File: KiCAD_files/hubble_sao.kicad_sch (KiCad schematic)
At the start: 41 parts, among them J1 Conn_02x03_Counter_Clockwise, J2 Conn_02x03_Odd_Even, Q1 DMP3099L-7, SW1 SW_Push_Shielded, U1 VEML3328, U2 LSM6DSO, U3 ATmega328PB-A, U4 AD8532, U5 AD8532

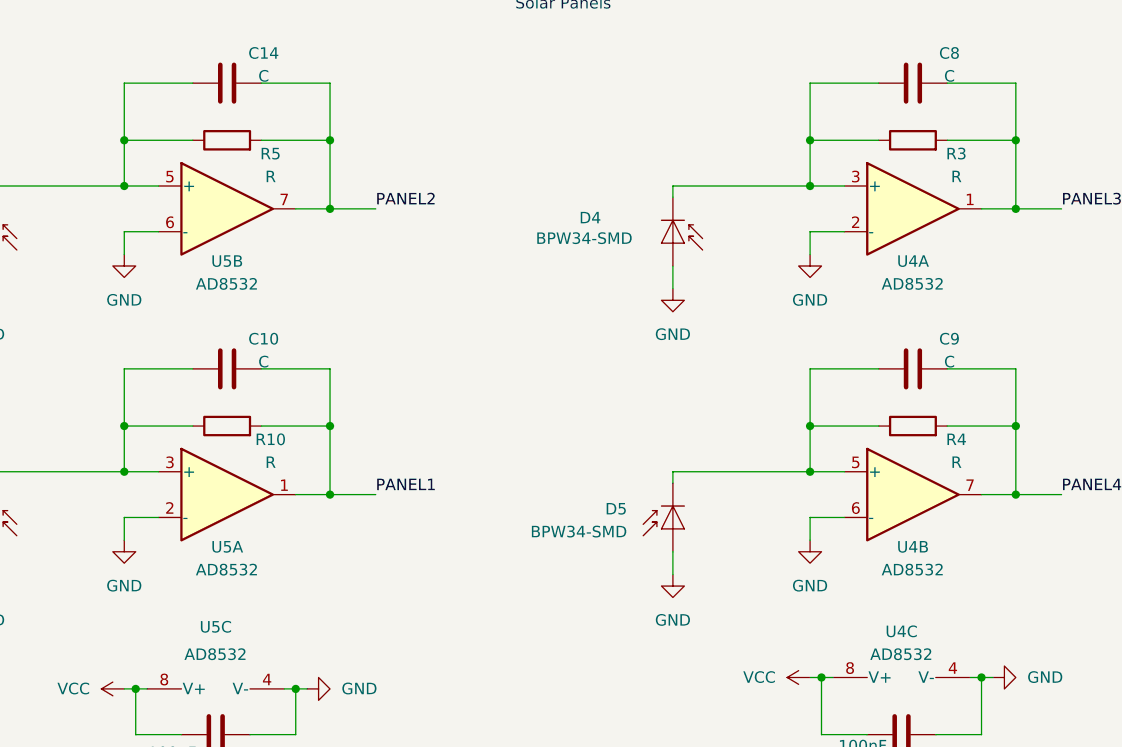
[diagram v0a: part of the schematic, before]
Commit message: Corrected the input wiring of the opamps (schematic & pcb)
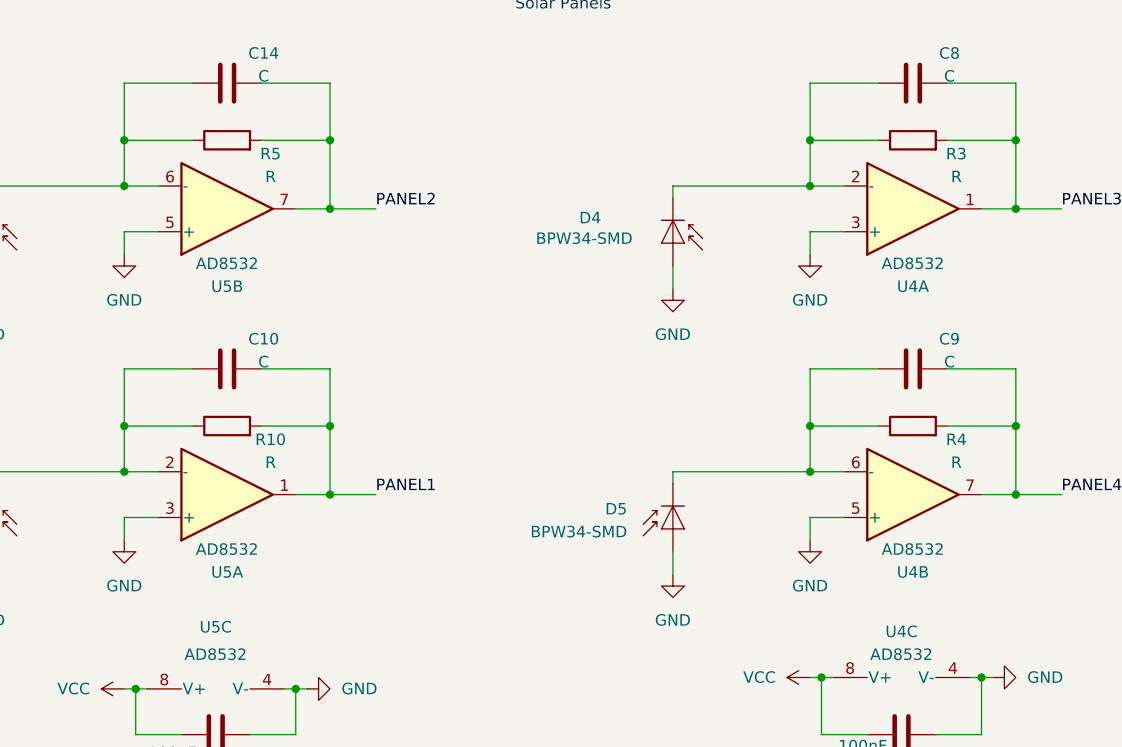
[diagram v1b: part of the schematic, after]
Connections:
- net GND: now also U4.3 (+), U4.5 (+), U5.3 (+), U5.5 (+); no longer U4.2 (-), U4.6 (-), U5.2 (-), U5.6 (-)
- net at C8.1, D4.1 (K), R3.1: now also U4.2 (-); no longer U4.3 (+)
- net at C9.1, D5.1 (K), R4.1: now also U4.6 (-); no longer U4.5 (+)
- net at C10.1, D3.1 (K), R10.1: now also U5.2 (-); no longer U5.3 (+)
- net at C14.1, D1.1 (K), R5.1: now also U5.6 (-); no longer U5.5 (+)
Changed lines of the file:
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@@
 		(lib_id "optical_sensors:AD8532")
 		(at 255.27 102.87 0)
+		(mirror x)
 		(unit 1)
 		(exclude_from_sim no)
@@
 		(dnp no)
 		(property "Reference" "U4"
-			(at 255.27 108.712 0)
+			(at 255.27 111.506 0)
 			(effects
 				(font
@@
 		)
 		(property "Value" "AD8532"
-			(at 255.27 111.252 0)
+			(at 255.27 108.966 0)
 			(effects
 				(font
@@
 		(lib_id "optical_sensors:AD8532")
 		(at 179.07 134.62 0)
+		(mirror x)
 		(unit 1)
 		(exclude_from_sim no)
@@
 		(dnp no)
 		(property "Reference" "U5"
-			(at 179.07 140.462 0)
+			(at 179.07 143.256 0)
 			(effects
 				(font
@@
 		)
 		(property "Value" "AD8532"
-			(at 179.07 143.002 0)
+			(at 179.07 140.716 0)
 			(effects
 				(font
@@
 		(lib_id "optical_sensors:AD8532")
 		(at 179.07 102.87 0)
+		(mirror x)
 		(unit 2)
 		(exclude_from_sim no)
@@
 		(dnp no)
 		(property "Reference" "U5"
-			(at 179.07 108.712 0)
+			(at 179.07 111.506 0)
 			(effects
 				(font
@@
 		)
 		(property "Value" "AD8532"
-			(at 179.07 111.252 0)
+			(at 179.07 108.966 0)
 			(effects
 				(font
@@
 		(lib_id "optical_sensors:AD8532")
 		(at 255.27 134.62 0)
+		(mirror x)
 		(unit 2)
 		(exclude_from_sim no)
@@
 		(dnp no)
 		(property "Reference" "U4"
-			(at 255.27 140.462 0)
+			(at 255.27 143.256 0)
 			(effects
 				(font
@@
 		)
 		(property "Value" "AD8532"
-			(at 255.27 143.002 0)
+			(at 255.27 140.716 0)
 			(effects
 				(font

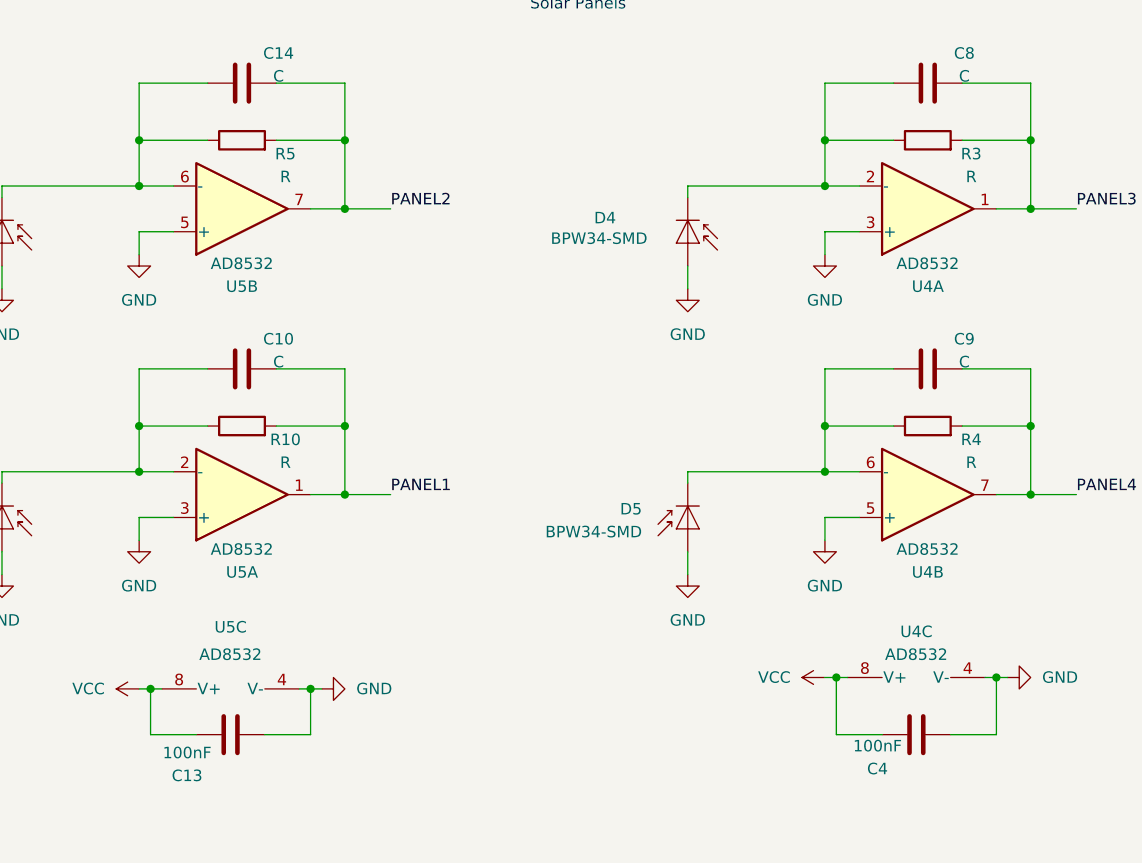
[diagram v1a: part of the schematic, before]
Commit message: Changed opamp from AD8532 to TLV9062D
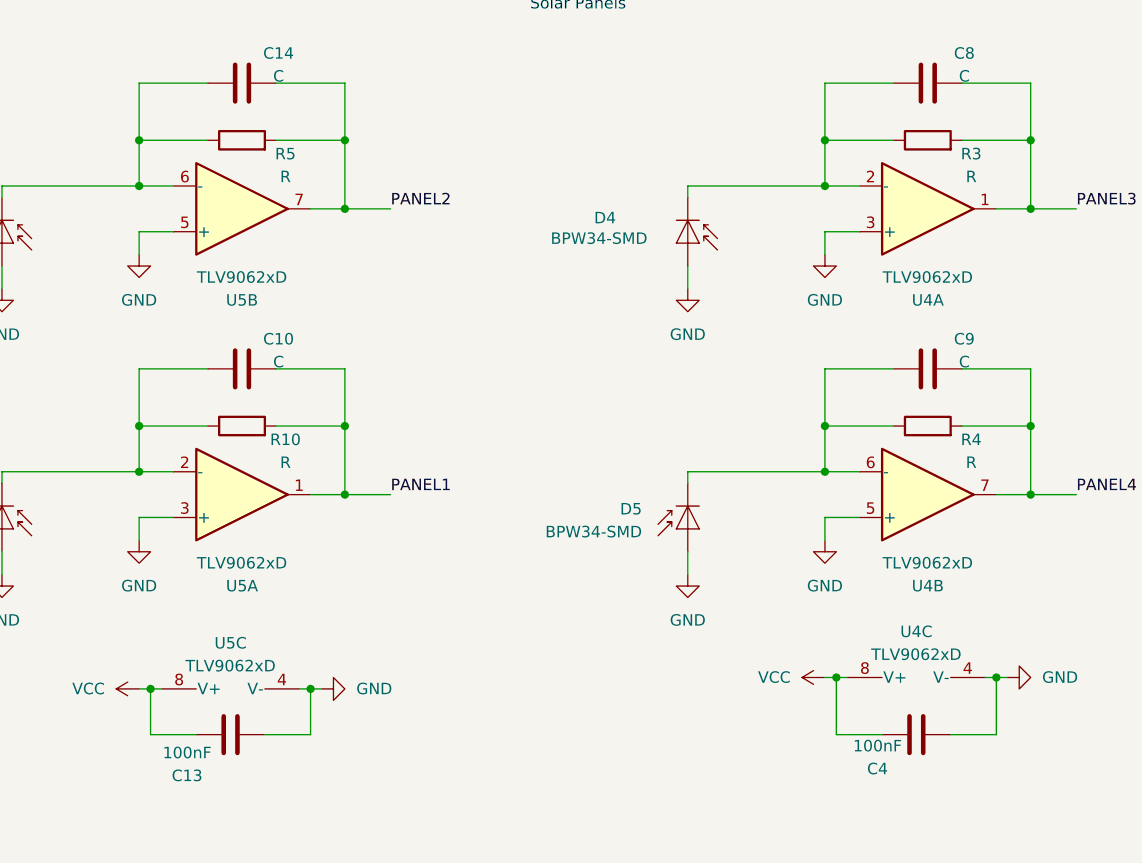
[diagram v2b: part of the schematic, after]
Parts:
- removed U4, U5: AD8532, Package_SO:SOIC-8_3.9x4.9mm_P1.27mm, symbol optical_sensors:AD8532
- added U4, U5: TLV9062xD, Package_SO:SOIC-8_3.9x4.9mm_P1.27mm, symbol Amplifier_Operational:TLV9062xD
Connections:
- net GND: now also U4.3 (+), U4.4 (V-), U4.5 (+), U5.3 (+), U5.4 (V-), U5.5 (+)
- net PANEL1: now also U5.1
- net PANEL2: now also U5.7
- net PANEL3: now also U4.1
- net PANEL4: now also U4.7
- net VCC: now also U4.8 (V+), U5.8 (V+)
- net at C8.1, D4.1 (K), R3.1: now also U4.2 (-)
- net at C9.1, D5.1 (K), R4.1: now also U4.6 (-)
- net at C10.1, D3.1 (K), R10.1: now also U5.2 (-)
- net at C14.1, D1.1 (K), R5.1: now also U5.6 (-)

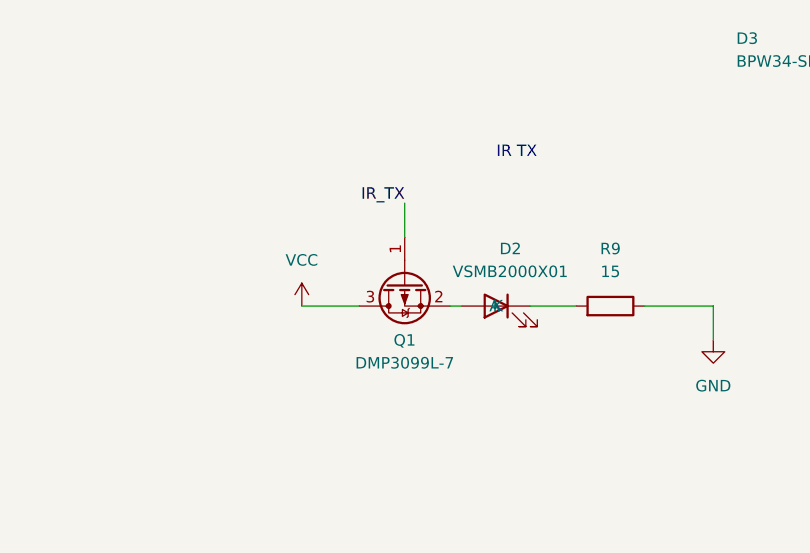
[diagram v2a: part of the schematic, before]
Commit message: FIX: Corrected the pMOSFET wiring. Fixes #1
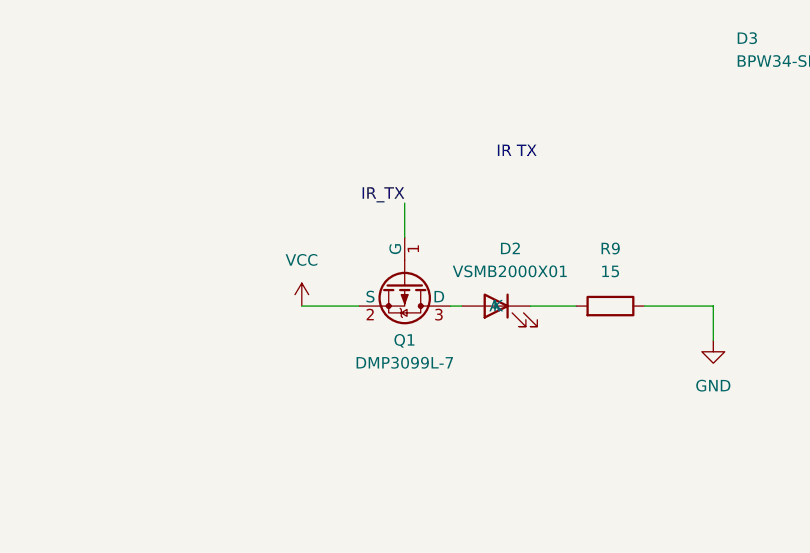
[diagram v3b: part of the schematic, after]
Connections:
- net VCC: now also Q1.2 (S); no longer Q1.3 (D)
- net at D2.2 (A): now also Q1.3 (D); no longer Q1.2 (S)
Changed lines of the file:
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@@
 	(symbol
 		(lib_id "Device:Q_PMOS_GSD")
-		(at 100.33 162.56 90)
-		(mirror x)
+		(at 100.33 162.56 270)
 		(unit 1)
 		(exclude_from_sim no)
@@
 		)
 		(property "Footprint" "Package_TO_SOT_SMD:SOT-23"
-			(at 97.79 167.64 0)
+			(at 102.87 167.64 0)
 			(effects
 				(font

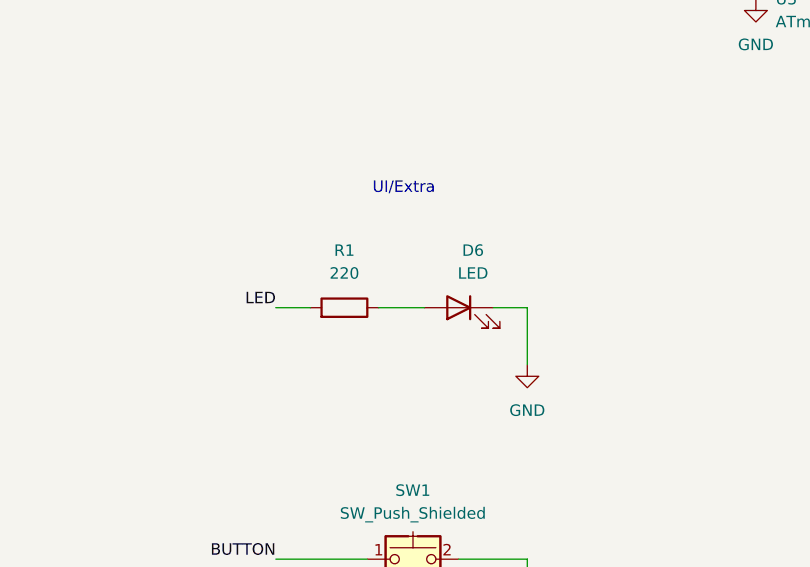
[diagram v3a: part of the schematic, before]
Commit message: Simplified the blinky LED's traces
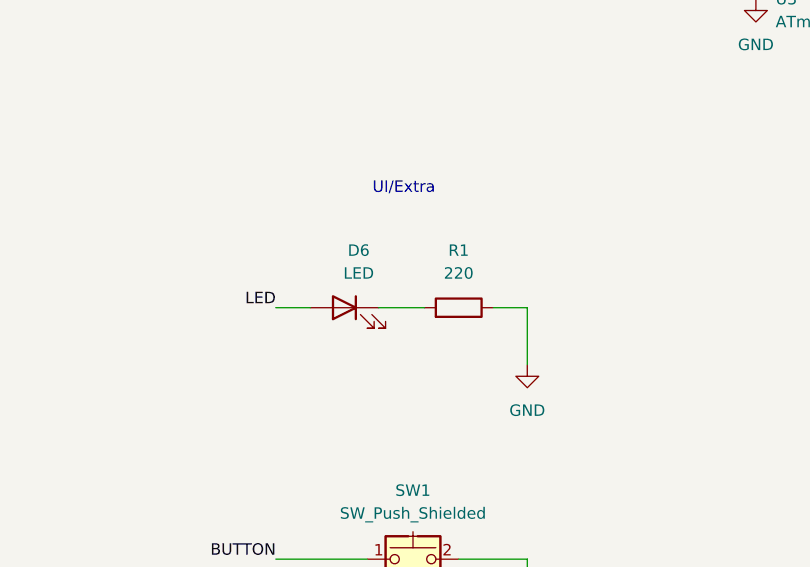
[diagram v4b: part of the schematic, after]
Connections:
- net GND: now also R1.1; no longer D6.1 (K)
- net LED: now also D6.2 (A); no longer R1.2
- new net: D6.1 (K), R1.2
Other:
- moved on the sheet: D6, R1
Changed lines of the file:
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@@
 	(symbol
 		(lib_id "Device:R")
-		(at 30.48 151.13 270)
+		(at 43.18 151.13 270)
 		(mirror x)
 		(unit 1)
@@
 		(fields_autoplaced yes)
 		(property "Reference" "R1"
-			(at 30.48 144.78 90)
+			(at 43.18 144.78 90)
 			(effects
 				(font
@@
 		)
 		(property "Value" "220"
-			(at 30.48 147.32 90)
+			(at 43.18 147.32 90)
 			(effects
 				(font
@@
 		)
 		(property "Footprint" "Resistor_SMD:R_1206_3216Metric_Pad1.30x1.75mm_HandSolder"
-			(at 30.48 152.908 90)
+			(at 43.18 152.908 90)
 			(effects
 				(font
@@
 		)
 		(property "Datasheet" "~"
-			(at 30.48 151.13 0)
+			(at 43.18 151.13 0)
 			(effects
 				(font
@@
 		)
 		(property "Description" "Resistor"
-			(at 30.48 151.13 0)
+			(at 43.18 151.13 0)
 			(effects
 				(font
@@
 	(symbol
 		(lib_id "Device:LED")
-		(at 43.18 151.13 0)
+		(at 30.48 151.13 0)
 		(mirror y)
 		(unit 1)
@@
 		(fields_autoplaced yes)
 		(property "Reference" "D6"
-			(at 44.7675 144.78 0)
+			(at 32.0675 144.78 0)
 			(effects
 				(font
@@
 		)
 		(property "Value" "LED"
-			(at 44.7675 147.32 0)
+			(at 32.0675 147.32 0)
 			(effects
 				(font
@@
 		)
 		(property "Footprint" "LED_SMD:LED_1206_3216Metric_ReverseMount_Hole1.8x2.4mm"
-			(at 43.18 151.13 0)
+			(at 30.48 151.13 0)
 			(effects
 				(font
@@
 		)
 		(property "Datasheet" "~"
-			(at 43.18 151.13 0)
+			(at 30.48 151.13 0)
 			(effects
 				(font
@@
 		)
 		(property "Description" "Light emitting diode"
-			(at 43.18 151.13 0)
-			(effects
-				(font
+			(at 30.48 151.13 0)
+			(effects
+				(font

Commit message: Replaced some 1206 resistors by 0805s to tighten up the PCB
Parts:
- R1, R10, R3, R4, R5: footprint Resistor_SMD:R_1206_3216Metric_Pad1.30x1.75mm_HandSolder -> Resistor_SMD:R_0805_2012Metric_Pad1.20x1.40mm_HandSolder
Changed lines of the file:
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@@
 			)
 		)
-		(property "Footprint" "Resistor_SMD:R_1206_3216Metric_Pad1.30x1.75mm_HandSolder"
+		(property "Footprint" "Resistor_SMD:R_0805_2012Metric_Pad1.20x1.40mm_HandSolder"
 			(at 179.07 97.028 90)
 			(effects
@@
 			)
 		)
-		(property "Footprint" "Resistor_SMD:R_1206_3216Metric_Pad1.30x1.75mm_HandSolder"
+		(property "Footprint" "Resistor_SMD:R_0805_2012Metric_Pad1.20x1.40mm_HandSolder"
 			(at 255.27 128.778 90)
 			(effects
@@
 			)
 		)
-		(property "Footprint" "Resistor_SMD:R_1206_3216Metric_Pad1.30x1.75mm_HandSolder"
+		(property "Footprint" "Resistor_SMD:R_0805_2012Metric_Pad1.20x1.40mm_HandSolder"
 			(at 43.18 152.908 90)
 			(effects
@@
 			)
 		)
-		(property "Footprint" "Resistor_SMD:R_1206_3216Metric_Pad1.30x1.75mm_HandSolder"
+		(property "Footprint" "Resistor_SMD:R_0805_2012Metric_Pad1.20x1.40mm_HandSolder"
 			(at 255.27 97.028 90)
 			(effects
@@
 			)
 		)
-		(property "Footprint" "Resistor_SMD:R_1206_3216Metric_Pad1.30x1.75mm_HandSolder"
+		(property "Footprint" "Resistor_SMD:R_0805_2012Metric_Pad1.20x1.40mm_HandSolder"
 			(at 179.07 128.778 90)
 			(effects

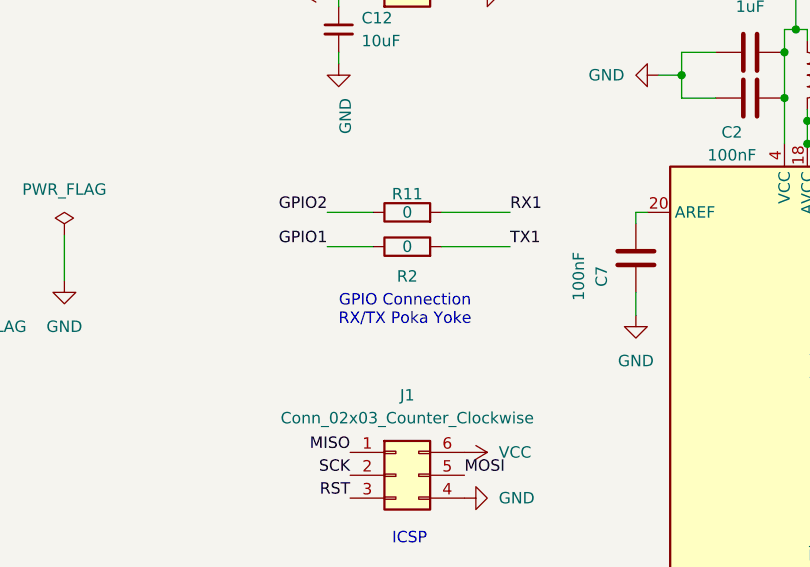
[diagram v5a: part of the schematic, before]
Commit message: Changed RX/TX resistors to 470Ohm for short circuit protection
Fixes #4
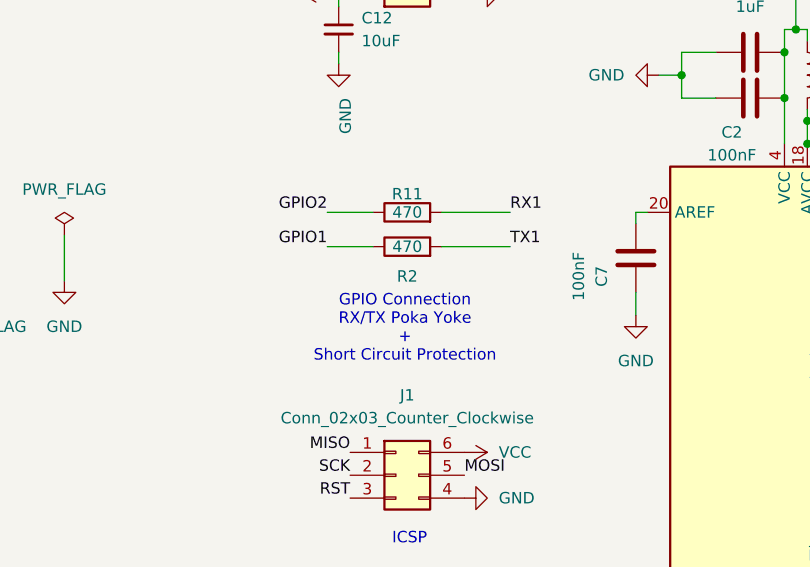
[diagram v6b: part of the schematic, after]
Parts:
- R11, R2: value 0 -> 470
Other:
- note added: "GPIO Connection RX/TX Poka Yoke + Short Circuit Protection"
- note removed: "GPIO Connection RX/TX Poka Yoke"
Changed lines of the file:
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@@
 		)
 	)
-	(text "GPIO Connection\nRX/TX Poka Yoke"
+	(text "GPIO Connection\nRX/TX Poka Yoke\n+\nShort Circuit Protection"
 		(exclude_from_sim no)
-		(at 34.036 59.182 0)
+		(at 34.036 61.214 0)
 		(effects
 			(font
@@
 			)
 		)
-		(property "Value" "0"
+		(property "Value" "470"
 			(at 34.29 52.07 90)
 			(effects
@@
 			)
 		)
-		(property "Value" "0"
+		(property "Value" "470"
 			(at 34.29 48.26 90)
 			(effects
